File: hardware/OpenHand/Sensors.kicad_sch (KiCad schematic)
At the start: 69 parts, among them U6 LM324, U7 LM324, U8 ADS1115IDGS

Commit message: Update schm and pcb
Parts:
- removed JP9: JMPR_I2C_ADC_SDA, Jumper:SolderJumper-2_P1.3mm_Bridged_RoundedPad1.0x1.5mm, symbol Jumper:SolderJumper_2_Bridged
- removed JP9: JMPR_I2C_ADC_SCL, Jumper:SolderJumper-2_P1.3mm_Bridged_RoundedPad1.0x1.5mm, symbol Jumper:SolderJumper_2_Bridged
- added JP9: JMPR_I2C_ADC_SCL, Jumper:SolderJumper-2_P1.3mm_Bridged_RoundedPad1.0x1.5mm, symbol Jumper:SolderJumper_2_Bridged
- added JP9: JMPR_I2C_ADC_SDA, Jumper:SolderJumper-2_P1.3mm_Bridged_RoundedPad1.0x1.5mm, symbol Jumper:SolderJumper_2_Bridged
- added R52: 10k, Resistor_SMD:R_0805_2012Metric_Pad1.20x1.40mm_HandSolder, symbol Device:R
- added TP50: TP_TRIM_3, symbol Connector:TestPoint_Small
- added TP50: TP_TRIM_2, symbol Connector:TestPoint_Small
- added TP50: TP_TRIM_4, symbol Connector:TestPoint_Small
- added TP50: TP_ADC_RDY, symbol Connector:TestPoint_Small
- added TP50: TP_TRIM_1, symbol Connector:TestPoint_Small
- added U8: ADS1115IDGS, Package_SO:TSSOP-10_3x3mm_P0.5mm, symbol Analog_ADC:ADS1115IDGS
- renumbered C26 to C25, C25 to C26, R20 to R22, R21 to R23, R22 to R24, R23 to R25, R24 to R26, R25 to R27, R26 to R28, R28 to R29, R27 to R30, R29 to R31, R30 to R32, R31 to R33, R32 to R34, R33 to R35, R34 to R36, R35 to R37, R36 to R38, R37 to R39, R38 to R40, R39 to R41, R40 to R42, R42 to R43, R41 to R44, R43 to R45, R44 to R46, R45 to R47, R47 to R48, R48 to R49, R46 to R50, R49 to R51, R50 to R53, R53 to R54, R54 to R55, U8 to U9
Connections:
- net +3V3: now also R52.2, U8.1 (ADDR), U8.8 (VDD)
- net Earth: now also U8.3 (GND)
- net UC_SCL: now also JP9.2 (B)
- net UC_SDA: now also JP9.1 (A)
- net ADC_SDA: now reaches U9.9 (SDA)
- net ADC_SDA: now also JP9.2 (B), U8.9 (SDA)
- net ADC_SCL: now reaches U9.10 (SCL)
- net ADC_SCL: now also JP9.1 (A), U8.10 (SCL)
- net ADC_ALERT_RDY renamed ADC_1_ALERT_RDY
- new net ADC_2_ALERT_RDY: R52.1, TP50.1, U8.2 (ALERT/RDY)
- new net BTN_1: TP50.1, U8.7 (AIN3)
- new net TRIM_POT_1: TP50.1, U8.4 (AIN0)
- new net TRIM_POT_2: TP50.1, U8.5 (AIN1)
- new net TRIM_POT_3: TP50.1, U8.6 (AIN2)
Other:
- note added: "POT ANALOG INPUTS"

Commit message: Update schm and pcb
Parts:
- TP50: footprint (none) -> TestPoint:TestPoint_Pad_D1.0mm

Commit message: update schm and pcb again
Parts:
- removed TP50: TP_EMG_2_UC, TestPoint:TestPoint_Pad_D1.0mm, symbol Connector:TestPoint_Small
- removed TP50: TP_EMG_1_UC, TestPoint:TestPoint_Pad_D1.0mm, symbol Connector:TestPoint_Small
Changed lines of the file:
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@@
   (junction (at 226.06 68.58) (diameter 0) (color 0 0 0 0)
   )
-  (junction (at 128.905 88.9) (diameter 0) (color 0 0 0 0)
-  )
   (junction (at 103.505 99.06) (diameter 0) (color 0 0 0 0)
   )
@@
   (junction (at 39.37 83.82) (diameter 0) (color 0 0 0 0)
   )
-  (junction (at 262.89 87.63) (diameter 0) (color 0 0 0 0)
-  )
   (junction (at 182.88 50.8) (diameter 0) (color 0 0 0 0)
   )
@@
     (stroke (width 0) (type default))
   )
-  (wire (pts (xy 128.905 88.9) (xy 132.08 88.9))
-    (stroke (width 0) (type default))
-  )
   (wire (pts (xy 126.365 104.775) (xy 126.365 102.235))
     (stroke (width 0) (type default))
@@
     (stroke (width 0) (type default))
   )
-  (wire (pts (xy 262.89 87.63) (xy 265.43 87.63))
+  (wire (pts (xy 260.35 87.63) (xy 265.43 87.63))
     (stroke (width 0) (type default))
   )
@@
     (stroke (width 0) (type default))
   )
-  (wire (pts (xy 126.365 88.9) (xy 128.905 88.9))
+  (wire (pts (xy 126.365 88.9) (xy 132.08 88.9))
     (stroke (width 0) (type default))
   )
@@
     (stroke (width 0) (type default))
   )
-  (wire (pts (xy 260.35 87.63) (xy 262.89 87.63))
-    (stroke (width 0) (type default))
-  )
   (wire (pts (xy 233.68 36.83) (xy 213.36 36.83))
     (stroke (width 0) (type default))
@@
     (stroke (width 0) (type default))
   )
-  (wire (pts (xy 128.905 83.185) (xy 128.905 88.9))
-    (stroke (width 0) (type default))
-  )
   (wire (pts (xy 260.35 93.98) (xy 260.35 95.25))
     (stroke (width 0) (type default))
@@
     (stroke (width 0) (type default))
   )
-  (wire (pts (xy 262.89 81.915) (xy 262.89 87.63))
-    (stroke (width 0) (type default))
-  )
   (wire (pts (xy 124.46 27.94) (xy 124.46 25.4))
     (stroke (width 0) (type default))
@@
         )
         (path "/f1fbd835-8408-4592-854c-2fbec9d052ec/286dde41-8068-419e-b7de-6276970410d8"
-          (reference "TP42") (unit 1)
+          (reference "TP38") (unit 1)
         )
       )
@@
         )
         (path "/f1fbd835-8408-4592-854c-2fbec9d052ec/286dde41-8068-419e-b7de-6276970410d8"
-          (reference "TP56") (unit 1)
+          (reference "TP52") (unit 1)
         )
       )
@@
         )
         (path "/f1fbd835-8408-4592-854c-2fbec9d052ec/286dde41-8068-419e-b7de-6276970410d8"
-          (reference "TP55") (unit 1)
+          (reference "TP51") (unit 1)
         )
       )
@@
         )
         (path "/f1fbd835-8408-4592-854c-2fbec9d052ec/286dde41-8068-419e-b7de-6276970410d8"
-          (reference "TP50") (unit 1)
+          (reference "TP46") (unit 1)
         )
       )
@@
         )
         (path "/f1fbd835-8408-4592-854c-2fbec9d052ec/286dde41-8068-419e-b7de-6276970410d8"
-          (reference "TP53") (unit 1)
+          (reference "TP49") (unit 1)
         )
       )
@@
         )
         (path "/f1fbd835-8408-4592-854c-2fbec9d052ec/286dde41-8068-419e-b7de-6276970410d8"
-          (reference "TP52") (unit 1)
+          (reference "TP48") (unit 1)
         )
       )
@@
         )
         (path "/f1fbd835-8408-4592-854c-2fbec9d052ec/286dde41-8068-419e-b7de-6276970410d8"
-          (reference "TP46") (unit 1)
+          (reference "TP42") (unit 1)
         )
       )
@@
         )
         (path "/f1fbd835-8408-4592-854c-2fbec9d052ec/286dde41-8068-419e-b7de-6276970410d8"
-          (reference "TP49") (unit 1)
+          (reference "TP45") (unit 1)
         )
       )
@@
         )
         (path "/f1fbd835-8408-4592-854c-2fbec9d052ec/286dde41-8068-419e-b7de-6276970410d8"
-          (reference "TP45") (unit 1)
+          (reference "TP41") (unit 1)
         )
       )
@@
     )
   )
-  (symbol (lib_id "Connector:TestPoint_Small") (at 262.89 81.915 180) (unit 1)
-    (in_bom yes) (on_board yes) (dnp no)
-    (property "Reference" "TP50" (at 262.89 79.375 0)
-      (effects (font (size 0.8 0.8)))
-    )
-    (property "Value" "TP_EMG_2_UC" (at 262.89 80.645 0)
-      (effects (font (size 0.8 0.8)))
-    )
-    (property "Footprint" "TestPoint:TestPoint_Pad_D1.0mm" (at 257.81 81.915 0)
-      (effects (font (size 1.27 1.27)) hide)
-    )
-    (property "Datasheet" "~" (at 257.81 81.915 0)
-      (effects (font (size 1.27 1.27)) hide)
-    )
-    (pin "1")
-    (instances
-      (project "OpenHand"
-        (path "/f1fbd835-8408-4592-854c-2fbec9d052ec/20793231-6e6d-417f-8f1f-2d40174b5a27"
-          (reference "TP50") (unit 1)
-        )
-        (path "/f1fbd835-8408-4592-854c-2fbec9d052ec"
-          (reference "TP4") (unit 1)
-        )
-        (path "/f1fbd835-8408-4592-854c-2fbec9d052ec/286dde41-8068-419e-b7de-6276970410d8"
-          (reference "TP43") (unit 1)
-        )
-      )
-    )
-  )
   (symbol (lib_id "power:Earth") (at 190.5 102.87 0) (unit 1)
     (in_bom yes) (on_board yes) (dnp no) (fields_autoplaced)
@@
         )
         (path "/f1fbd835-8408-4592-854c-2fbec9d052ec/286dde41-8068-419e-b7de-6276970410d8"
-          (reference "TP51") (unit 1)
-        )
-      )
-    )
-  )
-  (symbol (lib_id "Connector:TestPoint_Small") (at 128.905 83.185 180) (unit 1)
-    (in_bom yes) (on_board yes) (dnp no)
-    (property "Reference" "TP50" (at 128.905 80.645 0)
-      (effects (font (size 0.8 0.8)))
-    )
-    (property "Value" "TP_EMG_1_UC" (at 128.905 81.915 0)
-      (effects (font (size 0.8 0.8)))
-    )
-    (property "Footprint" "TestPoint:TestPoint_Pad_D1.0mm" (at 123.825 83.185 0)
-      (effects (font (size 1.27 1.27)) hide)
-    )
-    (property "Datasheet" "~" (at 123.825 83.185 0)
-      (effects (font (size 1.27 1.27)) hide)
-    )
-    (pin "1")
-    (instances
-      (project "OpenHand"
-        (path "/f1fbd835-8408-4592-854c-2fbec9d052ec/20793231-6e6d-417f-8f1f-2d40174b5a27"
-          (reference "TP50") (unit 1)
-        )
-        (path "/f1fbd835-8408-4592-854c-2fbec9d052ec"
-          (reference "TP4") (unit 1)
-        )
-        (path "/f1fbd835-8408-4592-854c-2fbec9d052ec/286dde41-8068-419e-b7de-6276970410d8"
-          (reference "TP44") (unit 1)
+          (reference "TP47") (unit 1)
         )
       )
@@
         )
         (path "/f1fbd835-8408-4592-854c-2fbec9d052ec/286dde41-8068-419e-b7de-6276970410d8"
-          (reference "TP41") (unit 1)
+          (reference "TP37") (unit 1)
         )
       )
@@
         )
         (path "/f1fbd835-8408-4592-854c-2fbec9d052ec/286dde41-8068-419e-b7de-6276970410d8"
-          (reference "TP40") (unit 1)
+          (reference "TP36") (unit 1)
         )
       )
@@
         )
         (path "/f1fbd835-8408-4592-854c-2fbec9d052ec/286dde41-8068-419e-b7de-6276970410d8"
-          (reference "TP47") (unit 1)
+          (reference "TP43") (unit 1)
         )
       )
@@
         )
         (path "/f1fbd835-8408-4592-854c-2fbec9d052ec/286dde41-8068-419e-b7de-6276970410d8"
-          (reference "TP39") (unit 1)
+          (reference "TP35") (unit 1)
         )
       )
@@
         )
         (path "/f1fbd835-8408-4592-854c-2fbec9d052ec/286dde41-8068-419e-b7de-6276970410d8"
-          (reference "TP54") (unit 1)
+          (reference "TP50") (unit 1)
         )
       )
@@
         )
         (path "/f1fbd835-8408-4592-854c-2fbec9d052ec/286dde41-8068-419e-b7de-6276970410d8"
-          (reference "TP48") (unit 1)
+          (reference "TP44") (unit 1)
         )
       )

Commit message: Major updates to schm and pcb, a bit better design
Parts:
- removed JP9: JMPR_I2C_ADC_SCL, Jumper:SolderJumper-2_P1.3mm_Bridged_RoundedPad1.0x1.5mm, symbol Jumper:SolderJumper_2_Bridged
- removed JP9: JMPR_I2C_ADC_SDA, Jumper:SolderJumper-2_P1.3mm_Bridged_RoundedPad1.0x1.5mm, symbol Jumper:SolderJumper_2_Bridged
- removed R52, R53, R55: 10k, Resistor_SMD:R_0805_2012Metric_Pad1.20x1.40mm_HandSolder, symbol Device:R
- removed R54: 47k, Resistor_SMD:R_0805_2012Metric_Pad1.20x1.40mm_HandSolder, symbol Device:R
- removed TP50: TP_HALL_03, TestPoint:TestPoint_Pad_D1.0mm, symbol Connector:TestPoint_Small
- removed TP50: TP_HALL_02, TestPoint:TestPoint_Pad_D1.0mm, symbol Connector:TestPoint_Small
- removed TP50: TP_TRIM_3, TestPoint:TestPoint_Pad_D1.0mm, symbol Connector:TestPoint_Small
- removed TP50: TP_BATT_SENSE, TestPoint:TestPoint_Pad_D1.0mm, symbol Connector:TestPoint_Small
- removed TP50 (x2): TP_ADC_RDY, TestPoint:TestPoint_Pad_D1.0mm, symbol Connector:TestPoint_Small
- removed TP50: TP_TRIM_2, TestPoint:TestPoint_Pad_D1.0mm, symbol Connector:TestPoint_Small
- removed TP50: TP_TRIM_4, TestPoint:TestPoint_Pad_D1.0mm, symbol Connector:TestPoint_Small
- removed TP50: TP_HALL_01, TestPoint:TestPoint_Pad_D1.0mm, symbol Connector:TestPoint_Small
- removed TP50: TP_TRIM_1, TestPoint:TestPoint_Pad_D1.0mm, symbol Connector:TestPoint_Small
- removed U8, U9: ADS1115IDGS, Package_SO:TSSOP-10_3x3mm_P0.5mm, symbol Analog_ADC:ADS1115IDGS
- C16: renamed from C15; footprint Capacitor_SMD:C_1206_3216Metric_Pad1.33x1.80mm_HandSolder -> Capacitor_SMD:C_0805_2012Metric
- C17: renamed from C16; footprint Capacitor_SMD:C_1206_3216Metric_Pad1.33x1.80mm_HandSolder -> Capacitor_SMD:C_0805_2012Metric
- C18: renamed from C19; footprint Capacitor_SMD:C_0805_2012Metric_Pad1.18x1.45mm_HandSolder -> Capacitor_SMD:C_0805_2012Metric
- C19: renamed from C20; footprint Capacitor_SMD:C_0805_2012Metric_Pad1.18x1.45mm_HandSolder -> Capacitor_SMD:C_0805_2012Metric
- C20: renamed from C17; footprint Capacitor_SMD:C_0805_2012Metric_Pad1.18x1.45mm_HandSolder -> Capacitor_SMD:C_0805_2012Metric
- C21: renamed from C18; footprint Capacitor_SMD:C_0805_2012Metric_Pad1.18x1.45mm_HandSolder -> Capacitor_SMD:C_0805_2012Metric
- C22, C24: footprint Capacitor_SMD:C_0805_2012Metric_Pad1.18x1.45mm_HandSolder -> Capacitor_SMD:C_0805_2012Metric
- C23: renamed from C21; footprint Capacitor_SMD:C_0805_2012Metric_Pad1.18x1.45mm_HandSolder -> Capacitor_SMD:C_0805_2012Metric
- C25: renamed from C23; footprint Capacitor_SMD:C_0805_2012Metric_Pad1.18x1.45mm_HandSolder -> Capacitor_SMD:C_0805_2012Metric
- C26: renamed from C25; footprint Capacitor_SMD:C_0805_2012Metric_Pad1.18x1.45mm_HandSolder -> Capacitor_SMD:C_0805_2012Metric
- C27: renamed from C26; footprint Capacitor_SMD:C_0805_2012Metric_Pad1.18x1.45mm_HandSolder -> Capacitor_SMD:C_0805_2012Metric
- R22: renamed from R23; footprint Resistor_SMD:R_0805_2012Metric_Pad1.20x1.40mm_HandSolder -> Resistor_SMD:R_0805_2012Metric
- R23: renamed from R25; footprint Resistor_SMD:R_0805_2012Metric_Pad1.20x1.40mm_HandSolder -> Resistor_SMD:R_0805_2012Metric
- R24: renamed from R22; footprint Resistor_SMD:R_0805_2012Metric_Pad1.20x1.40mm_HandSolder -> Resistor_SMD:R_0805_2012Metric
- R25: renamed from R24; footprint Resistor_SMD:R_0805_2012Metric_Pad1.20x1.40mm_HandSolder -> Resistor_SMD:R_0805_2012Metric
- R26: renamed from R27; footprint Resistor_SMD:R_0805_2012Metric_Pad1.20x1.40mm_HandSolder -> Resistor_SMD:R_0805_2012Metric
- R27: renamed from R26; footprint Resistor_SMD:R_0805_2012Metric_Pad1.20x1.40mm_HandSolder -> Resistor_SMD:R_0805_2012Metric
- R28: renamed from R30; footprint Resistor_SMD:R_0805_2012Metric_Pad1.20x1.40mm_HandSolder -> Resistor_SMD:R_0805_2012Metric
- R29: renamed from R31; footprint Resistor_SMD:R_0805_2012Metric_Pad1.20x1.40mm_HandSolder -> Resistor_SMD:R_0805_2012Metric
- R30: renamed from R28; footprint Resistor_SMD:R_0805_2012Metric_Pad1.20x1.40mm_HandSolder -> Resistor_SMD:R_0805_2012Metric
- R31: renamed from R29; footprint Resistor_SMD:R_0805_2012Metric_Pad1.20x1.40mm_HandSolder -> Resistor_SMD:R_0805_2012Metric
- R32: renamed from R34; footprint Resistor_SMD:R_0805_2012Metric_Pad1.20x1.40mm_HandSolder -> Resistor_SMD:R_0805_2012Metric
- R33: renamed from R35; footprint Resistor_SMD:R_0805_2012Metric_Pad1.20x1.40mm_HandSolder -> Resistor_SMD:R_0805_2012Metric
- R34: renamed from R37; footprint Resistor_SMD:R_0805_2012Metric_Pad1.20x1.40mm_HandSolder -> Resistor_SMD:R_0805_2012Metric
- R35: renamed from R32; footprint Resistor_SMD:R_0805_2012Metric_Pad1.20x1.40mm_HandSolder -> Resistor_SMD:R_0805_2012Metric
- R36: renamed from R33; footprint Resistor_SMD:R_0805_2012Metric_Pad1.20x1.40mm_HandSolder -> Resistor_SMD:R_0805_2012Metric
- R37: renamed from R36; footprint Resistor_SMD:R_0805_2012Metric_Pad1.20x1.40mm_HandSolder -> Resistor_SMD:R_0805_2012Metric
- R38: renamed from R39; footprint Resistor_SMD:R_0805_2012Metric_Pad1.20x1.40mm_HandSolder -> Resistor_SMD:R_0805_2012Metric
- R39: renamed from R38; footprint Resistor_SMD:R_0805_2012Metric_Pad1.20x1.40mm_HandSolder -> Resistor_SMD:R_0805_2012Metric
- R40: renamed from R41; footprint Resistor_SMD:R_0805_2012Metric_Pad1.20x1.40mm_HandSolder -> Resistor_SMD:R_0805_2012Metric
- R41: renamed from R40; footprint Resistor_SMD:R_0805_2012Metric_Pad1.20x1.40mm_HandSolder -> Resistor_SMD:R_0805_2012Metric
- R42, R48: footprint Resistor_SMD:R_0805_2012Metric_Pad1.20x1.40mm_HandSolder -> Resistor_SMD:R_0805_2012Metric
- R43: renamed from R44; footprint Resistor_SMD:R_0805_2012Metric_Pad1.20x1.40mm_HandSolder -> Resistor_SMD:R_0805_2012Metric
- R44: renamed from R45; footprint Resistor_SMD:R_0805_2012Metric_Pad1.20x1.40mm_HandSolder -> Resistor_SMD:R_0805_2012Metric
- R45: renamed from R43; footprint Resistor_SMD:R_0805_2012Metric_Pad1.20x1.40mm_HandSolder -> Resistor_SMD:R_0805_2012Metric
- R46: renamed from R47; footprint Resistor_SMD:R_0805_2012Metric_Pad1.20x1.40mm_HandSolder -> Resistor_SMD:R_0805_2012Metric
- R47: renamed from R46; footprint Resistor_SMD:R_0805_2012Metric_Pad1.20x1.40mm_HandSolder -> Resistor_SMD:R_0805_2012Metric
- R49: renamed from R51; footprint Resistor_SMD:R_0805_2012Metric_Pad1.20x1.40mm_HandSolder -> Resistor_SMD:R_0805_2012Metric
- R50: renamed from R49; footprint Resistor_SMD:R_0805_2012Metric_Pad1.20x1.40mm_HandSolder -> Resistor_SMD:R_0805_2012Metric
- R51: renamed from R50; footprint Resistor_SMD:R_0805_2012Metric_Pad1.20x1.40mm_HandSolder -> Resistor_SMD:R_0805_2012Metric
- renumbered D6 to D5, D5 to D6, RV5 to RV4, RV4 to RV5, U6 to U5, U7 to U6
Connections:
- net EMG_1_N renamed EMG_01_N
- net EMG_1_P renamed EMG_01_P
- net EMG_1_UC renamed EMG_01_UC
- net EMG_2_N renamed EMG_02_N
- net EMG_2_P renamed EMG_02_P
- net EMG_2_UC renamed EMG_02_UC
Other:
- note removed: "Battery voltage sensor 3x hall efect sensors (one per finger)"
- note removed: "OTHER SENSORS"
- note removed: "POT ANALOG INPUTS"
- note removed: "Up to 4 ICs per I2C line, connect ADDR line to ground, VDD, SDA, or SCL to select address"
- note removed: "Voltage divider: - max bat voltage 12.6V - gives us ~2.2V on output"
- moved on the sheet: C18, C19, C20, C21, C22, C23, C24, C25, C26, C27, D5, D6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

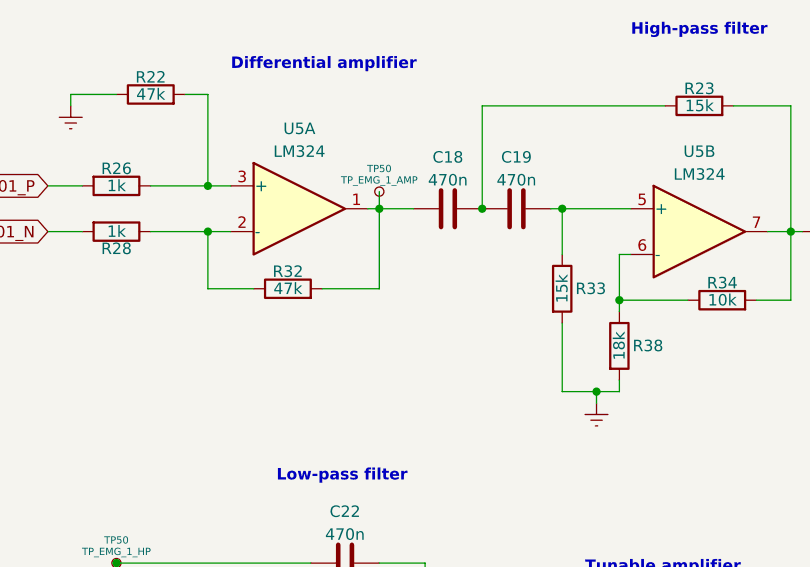
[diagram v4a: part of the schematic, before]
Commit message: Update PCB design/layout
Still WIP, routing traces currently
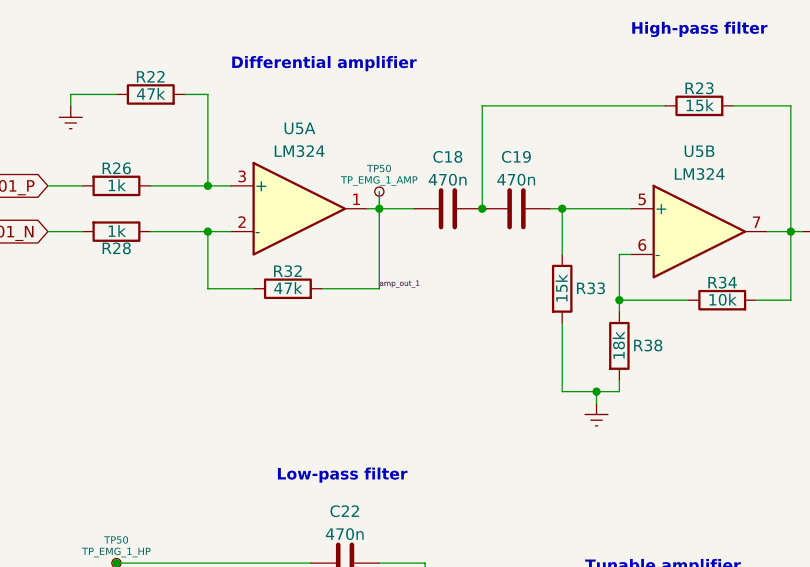
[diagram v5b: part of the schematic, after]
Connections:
- net amp_out_1: now reaches C18.1, R32.2, TP50.1, U5.1
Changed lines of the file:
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@@
     (effects (font (size 1.27 1.27) (thickness 0.254) bold) (justify left bottom))
+  )
+  (label "amp_out_1" (at 68.58 66.04 0) (fields_autoplaced)
+    (effects (font (size 0.6 0.6)) (justify left bottom))
   )
   (global_label "EMG_1_MIDPOINT" (shape output) (at 124.46 59.69 0) (fields_autoplaced)
